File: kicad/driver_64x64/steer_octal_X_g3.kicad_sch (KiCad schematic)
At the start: 66 parts

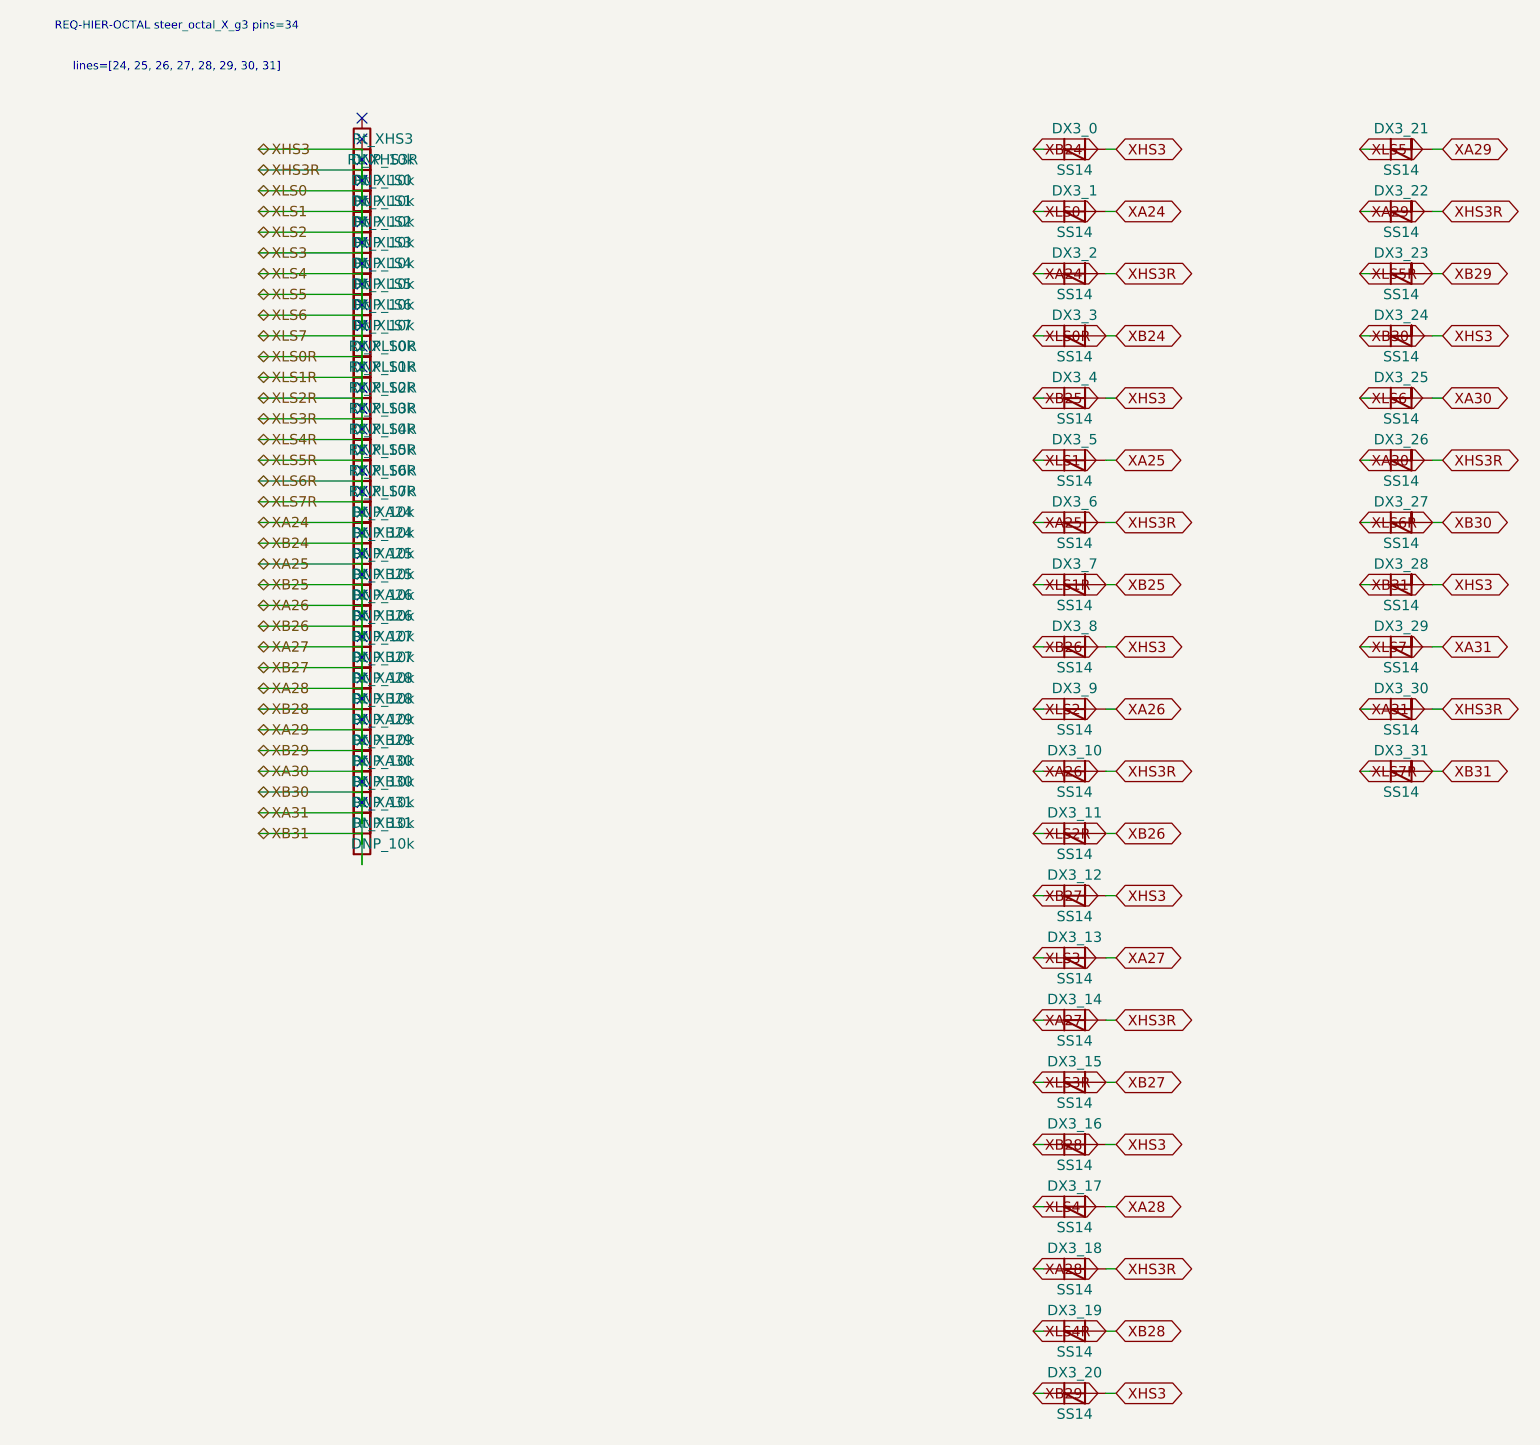
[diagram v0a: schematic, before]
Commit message: logical seperation into host and multiple decode/drive/steering boards
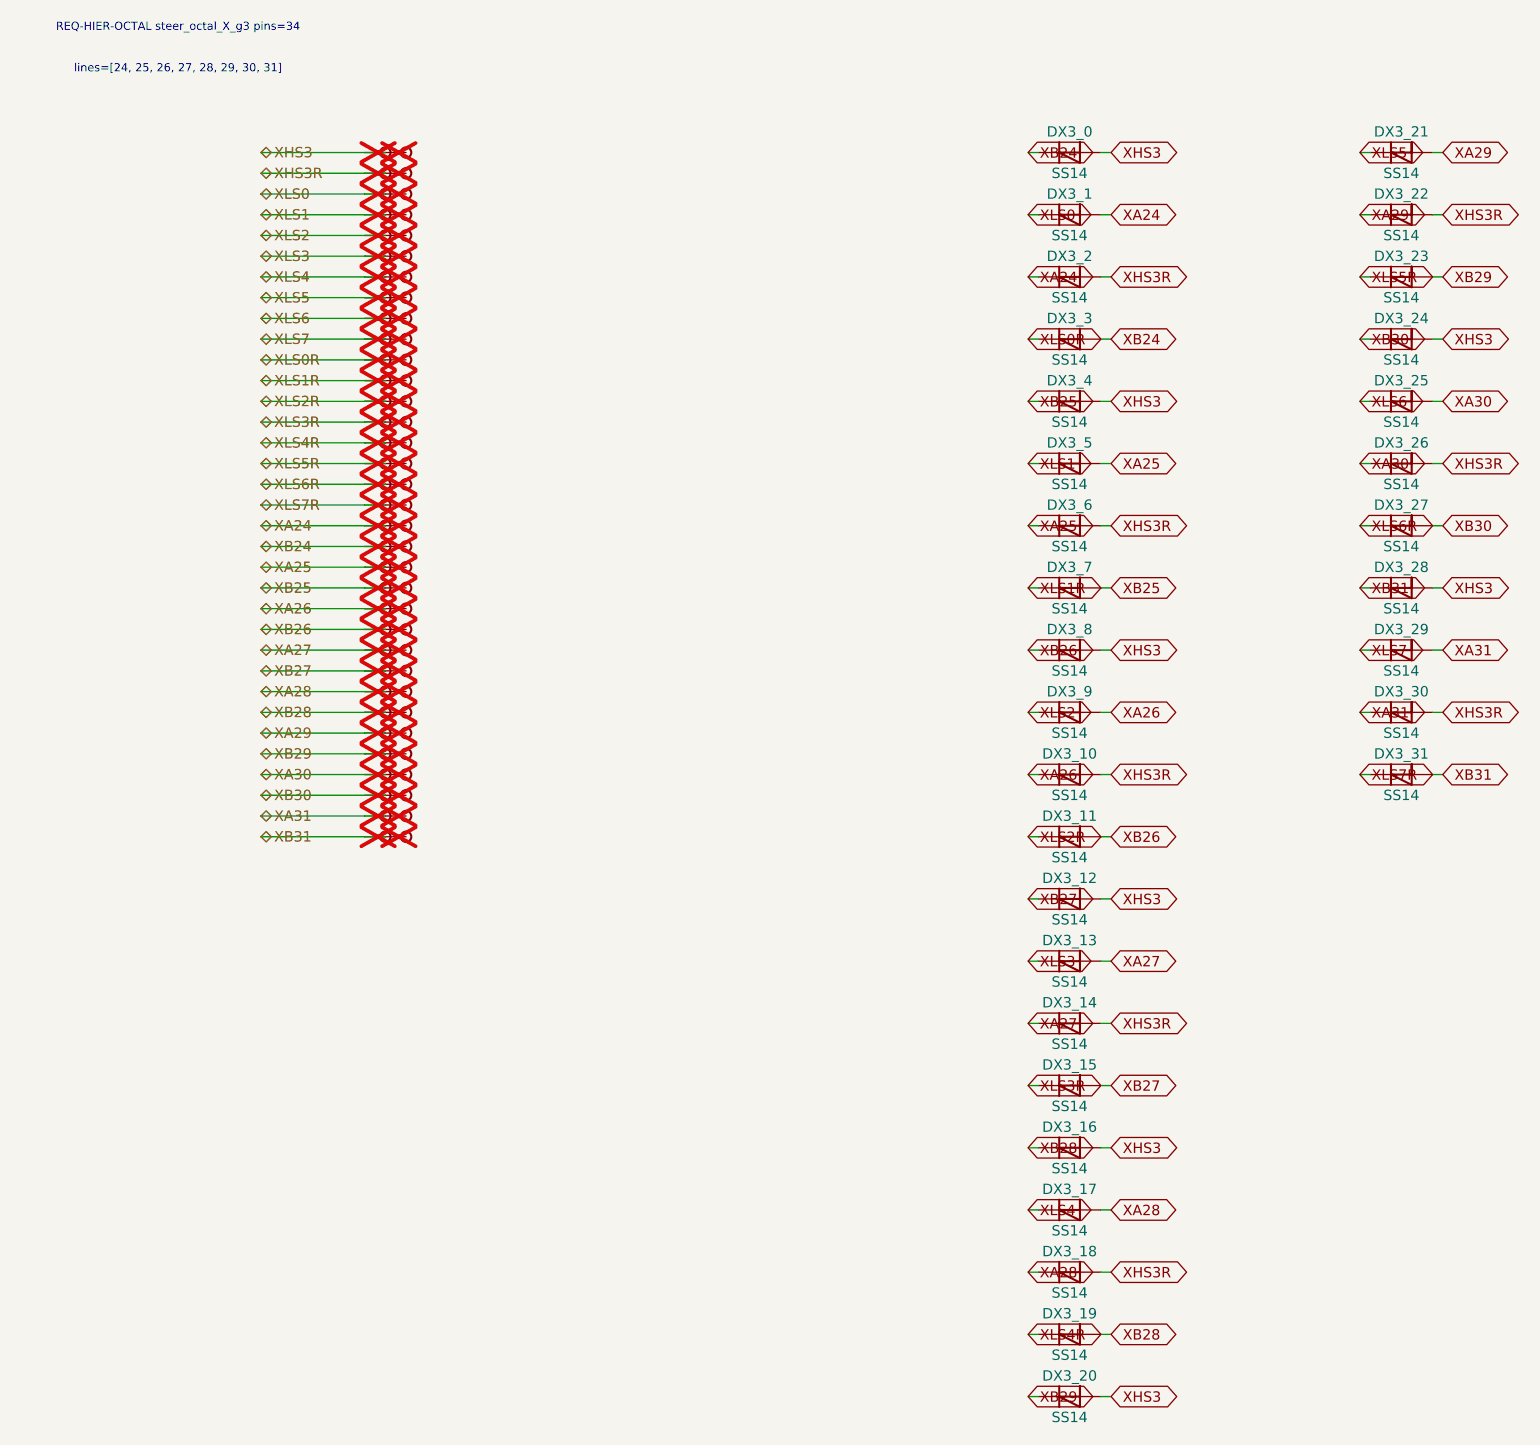
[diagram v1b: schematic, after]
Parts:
- removed Rt_XA24, Rt_XA25, Rt_XA26, Rt_XA27, Rt_XA28, Rt_XA29, Rt_XA30, Rt_XA31, Rt_XB24, Rt_XB25, Rt_XB26, Rt_XB27, Rt_XB28, Rt_XB29, Rt_XB30, Rt_XB31, Rt_XHS3, Rt_XHS3R, Rt_XLS0, Rt_XLS0R, Rt_XLS1, Rt_XLS1R, Rt_XLS2, Rt_XLS2R, Rt_XLS3, Rt_XLS3R, Rt_XLS4, Rt_XLS4R, Rt_XLS5, Rt_XLS5R, Rt_XLS6, Rt_XLS6R, Rt_XLS7, Rt_XLS7R: DNP_10k, symbol Device:R
- added TP_XA24, TP_XA24b, TP_XA25, TP_XA25b, TP_XA26, TP_XA26b, TP_XA27, TP_XA27b, TP_XA28, TP_XA28b, TP_XA29, TP_XA29b, TP_XA30, TP_XA30b, TP_XA31, TP_XA31b, TP_XB24, TP_XB24b, TP_XB25, TP_XB25b, TP_XB26, TP_XB26b, TP_XB27, TP_XB27b, TP_XB28, TP_XB28b, TP_XB29, TP_XB29b, TP_XB30, TP_XB30b, TP_XB31, TP_XB31b, TP_XHS3, TP_XHS3R, TP_XHS3Rb, TP_XHS3b, TP_XLS0, TP_XLS0R, TP_XLS0Rb, TP_XLS0b, TP_XLS1, TP_XLS1R, TP_XLS1Rb, TP_XLS1b, TP_XLS2, TP_XLS2R, TP_XLS2Rb, TP_XLS2b, TP_XLS3, TP_XLS3R, TP_XLS3Rb, TP_XLS3b, TP_XLS4, TP_XLS4R, TP_XLS4Rb, TP_XLS4b, TP_XLS5, TP_XLS5R, TP_XLS5Rb, TP_XLS5b, TP_XLS6, TP_XLS6R, TP_XLS6Rb, TP_XLS6b, TP_XLS7, TP_XLS7R, TP_XLS7Rb, TP_XLS7b: Stub, symbol CMR:Stub
- DX3_0, DX3_1, DX3_10, DX3_11, DX3_12, DX3_13, DX3_14, DX3_15, DX3_16, DX3_17, DX3_18, DX3_19, DX3_2, DX3_20, DX3_21, DX3_22, DX3_23, DX3_24, DX3_25, DX3_26, DX3_27, DX3_28, DX3_29, DX3_3, DX3_30, DX3_31, DX3_4, DX3_5, DX3_6, DX3_7, DX3_8, DX3_9: symbol Device:D_Schottky -> CMR:D_Schottky
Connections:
- net XA24: now also TP_XA24.1, TP_XA24b.1; no longer DX3_0.1 (K), DX3_0.2 (A), DX3_1.1 (K), DX3_10.1 (K), DX3_10.2 (A), DX3_11.1 (K), DX3_11.2 (A), DX3_12.1 (K), DX3_12.2 (A), DX3_13.1 (K), DX3_13.2 (A), DX3_14.1 (K), DX3_14.2 (A), DX3_15.1 (K), DX3_15.2 (A), DX3_16.1 (K), DX3_16.2 (A), DX3_17.1 (K), DX3_17.2 (A), DX3_18.1 (K), DX3_18.2 (A), DX3_19.1 (K), DX3_19.2 (A), DX3_2.2 (A), DX3_20.1 (K), DX3_20.2 (A), DX3_21.1 (K), DX3_21.2 (A), DX3_22.1 (K), DX3_22.2 (A), DX3_23.1 (K), DX3_23.2 (A), DX3_24.1 (K), DX3_24.2 (A), DX3_25.1 (K), DX3_25.2 (A), DX3_26.1 (K), DX3_26.2 (A), DX3_27.1 (K), DX3_27.2 (A), DX3_28.1 (K), DX3_28.2 (A), DX3_29.1 (K), DX3_29.2 (A), DX3_3.1 (K), DX3_3.2 (A), DX3_30.1 (K), DX3_30.2 (A), DX3_31.1 (K), DX3_31.2 (A), DX3_4.1 (K), DX3_4.2 (A), DX3_5.1 (K), DX3_5.2 (A), DX3_6.1 (K), DX3_6.2 (A), DX3_7.1 (K), DX3_7.2 (A), DX3_8.1 (K), DX3_8.2 (A), DX3_9.1 (K), DX3_9.2 (A)
- new net XA25: DX3_5.2 (A), DX3_6.1 (K), TP_XA25.1, TP_XA25b.1
- new net XA26: DX3_10.1 (K), DX3_9.2 (A), TP_XA26.1, TP_XA26b.1
- new net XA27: DX3_13.2 (A), DX3_14.1 (K), TP_XA27.1, TP_XA27b.1
- new net XA28: DX3_17.2 (A), DX3_18.1 (K), TP_XA28.1, TP_XA28b.1
- new net XA29: DX3_21.2 (A), DX3_22.1 (K), TP_XA29.1, TP_XA29b.1
- new net XA30: DX3_25.2 (A), DX3_26.1 (K), TP_XA30.1, TP_XA30b.1
- new net XA31: DX3_29.2 (A), DX3_30.1 (K), TP_XA31.1, TP_XA31b.1
- new net XB24: DX3_0.1 (K), DX3_3.2 (A), TP_XB24.1, TP_XB24b.1
- new net XB25: DX3_4.1 (K), DX3_7.2 (A), TP_XB25.1, TP_XB25b.1
- new net XB26: DX3_11.2 (A), DX3_8.1 (K), TP_XB26.1, TP_XB26b.1
- new net XB27: DX3_12.1 (K), DX3_15.2 (A), TP_XB27.1, TP_XB27b.1
- new net XB28: DX3_16.1 (K), DX3_19.2 (A), TP_XB28.1, TP_XB28b.1
- new net XB29: DX3_20.1 (K), DX3_23.2 (A), TP_XB29.1, TP_XB29b.1
- new net XB30: DX3_24.1 (K), DX3_27.2 (A), TP_XB30.1, TP_XB30b.1
- new net XB31: DX3_28.1 (K), DX3_31.2 (A), TP_XB31.1, TP_XB31b.1
- new net XHS3: DX3_0.2 (A), DX3_12.2 (A), DX3_16.2 (A), DX3_20.2 (A), DX3_24.2 (A), DX3_28.2 (A), DX3_4.2 (A), DX3_8.2 (A), TP_XHS3.1, TP_XHS3b.1
- new net XHS3R: DX3_10.2 (A), DX3_14.2 (A), DX3_18.2 (A), DX3_2.2 (A), DX3_22.2 (A), DX3_26.2 (A), DX3_30.2 (A), DX3_6.2 (A), TP_XHS3R.1, TP_XHS3Rb.1
- new net XLS0: DX3_1.1 (K), TP_XLS0.1, TP_XLS0b.1
- new net XLS0R: DX3_3.1 (K), TP_XLS0R.1, TP_XLS0Rb.1
- new net XLS1: DX3_5.1 (K), TP_XLS1.1, TP_XLS1b.1
- new net XLS1R: DX3_7.1 (K), TP_XLS1R.1, TP_XLS1Rb.1
- new net XLS2: DX3_9.1 (K), TP_XLS2.1, TP_XLS2b.1
- new net XLS2R: DX3_11.1 (K), TP_XLS2R.1, TP_XLS2Rb.1
- new net XLS3: DX3_13.1 (K), TP_XLS3.1, TP_XLS3b.1
- new net XLS3R: DX3_15.1 (K), TP_XLS3R.1, TP_XLS3Rb.1
- new net XLS4: DX3_17.1 (K), TP_XLS4.1, TP_XLS4b.1
- new net XLS4R: DX3_19.1 (K), TP_XLS4R.1, TP_XLS4Rb.1
- new net XLS5: DX3_21.1 (K), TP_XLS5.1, TP_XLS5b.1
- new net XLS5R: DX3_23.1 (K), TP_XLS5R.1, TP_XLS5Rb.1
- new net XLS6: DX3_25.1 (K), TP_XLS6.1, TP_XLS6b.1
- new net XLS6R: DX3_27.1 (K), TP_XLS6R.1, TP_XLS6Rb.1
- new net XLS7: DX3_29.1 (K), TP_XLS7.1, TP_XLS7b.1
- new net XLS7R: DX3_31.1 (K), TP_XLS7R.1, TP_XLS7Rb.1
- no-connect marks 34 -> 0
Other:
- moved on the sheet: DX3_0, DX3_1, DX3_10, DX3_11, DX3_12, DX3_13, DX3_14, DX3_15, DX3_16, DX3_17, DX3_18, DX3_19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
